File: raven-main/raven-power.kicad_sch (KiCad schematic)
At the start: 0 parts

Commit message: Added opamp circuits
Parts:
- added C10: 10uF, Capacitor_SMD:C_0402_1005Metric, symbol Device:C_Small
- added C11: 100nF, Capacitor_SMD:C_0402_1005Metric, symbol Device:C_Small
- added C12: 10nF, Capacitor_SMD:C_0402_1005Metric, symbol Device:C_Small
- added C4: 10pF, Capacitor_SMD:C_0402_1005Metric, symbol Device:C_Small
- added C5: 47uF, Capacitor_SMD:C_0402_1005Metric, symbol Device:C_Small
- added J1: XT60PW-M, AMASS_XT60PW-M, symbol iclr:XT60PW-M
- added R3: 226K, Resistor_SMD:R_0603_1608Metric, symbol Device:R
- added R4: 30k, Resistor_SMD:R_0603_1608Metric, symbol Device:R
- added R6: 31.6k, Resistor_SMD:R_0603_1608Metric, symbol Device:R
- added R7: 10k, Resistor_SMD:R_0603_1608Metric, symbol Device:R
- added U6: TPSM863257RDXR, RDX0007A-MFG, symbol TPSM863257RDXR:TPSM863257RDXR
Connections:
- new net: C12.1, R6.2, R7.1, U6.6 (EN)
- new net: C4.2, R3.2, R4.1, U6.7 (FB)
- new net 5V: C4.1, C5.1, R3.1, U6.3 (VOUT)
- new net BB_IN: C10.1, C11.1, J1.1 (+), R6.1, U6.1 (VIN)
- new net GND: C10.2, C11.2, C12.2, C5.2, J1.2 (-), R4.2, R7.2, U6.4 (PGND)
- no-connect marks 0 -> 2

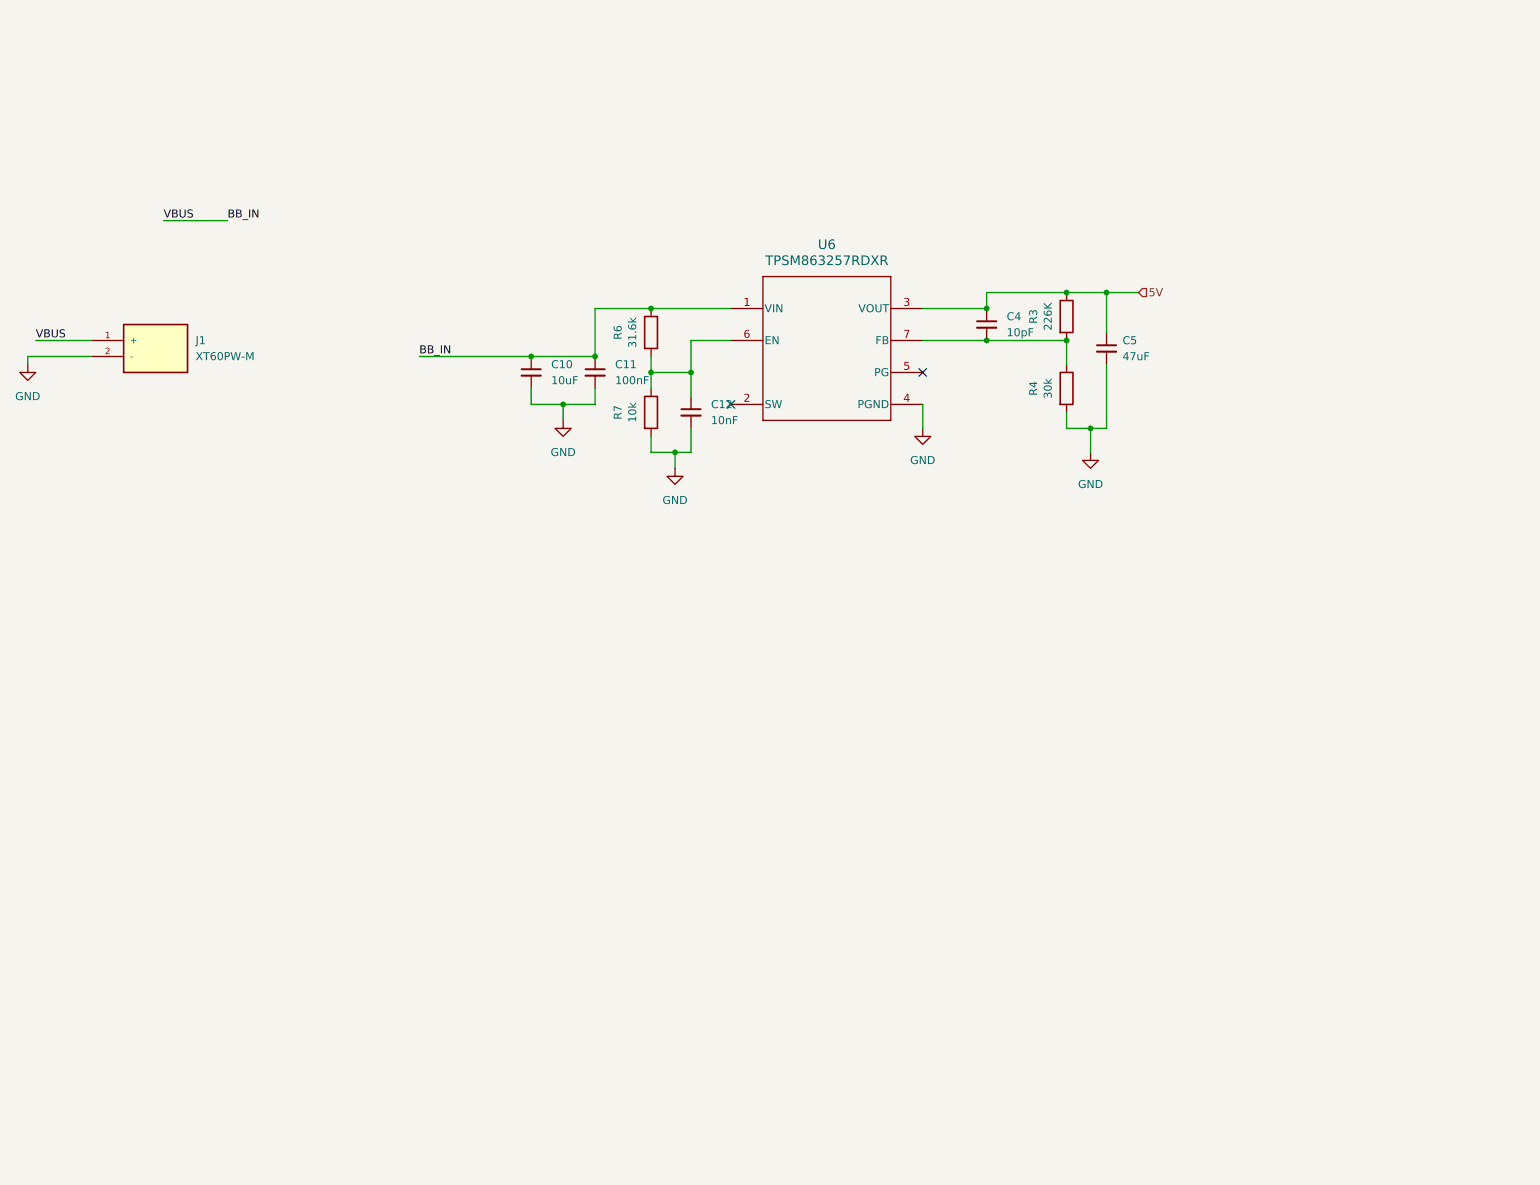
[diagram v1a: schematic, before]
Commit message: Added LDO Regulator
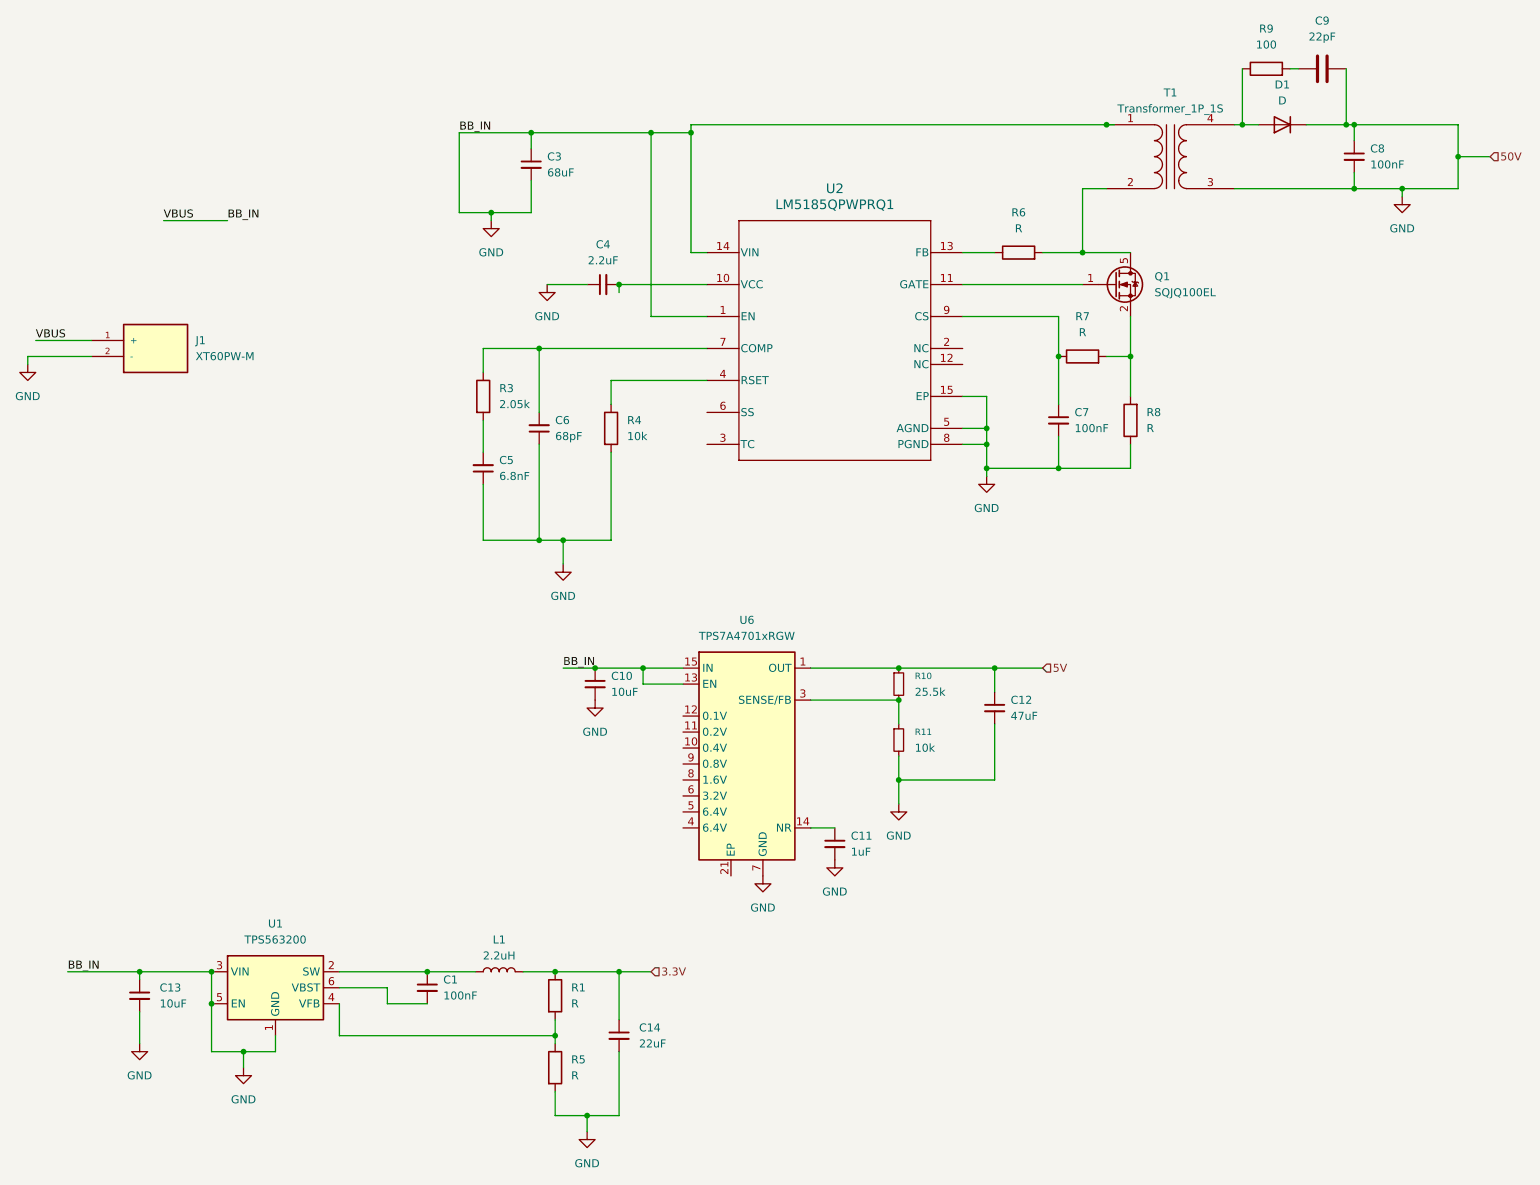
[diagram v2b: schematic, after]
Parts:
- removed U6: TPSM863257RDXR, RDX0007A-MFG, symbol TPSM863257RDXR:TPSM863257RDXR
- added C1, C7, C8: 100nF, symbol Device:C_Small
- added C13: 10uF, Capacitor_SMD:C_0402_1005Metric, symbol Device:C_Small
- added C14: 22uF, Capacitor_SMD:C_0402_1005Metric, symbol Device:C_Small
- added C3: 68uF, symbol Device:C_Small
- added C6: 68pF, symbol Device:C_Small
- added C9: 22pF, symbol Device:C
- added D1: D, symbol Device:D
- added L1: 2.2uH, symbol Device:L
- added Q1: SQJQ100EL, Package_TO_SOT_SMD:LFPAK88, symbol Transistor_FET:SQJQ100EL
- added R1, R5, R8: R, symbol Device:R
- added R10: 25.5k, symbol Device:R_Small
- added R11: 10k, symbol Device:R_Small
- added R9: 100, symbol Device:R
- added T1: Transformer_1P_1S, symbol Device:Transformer_1P_1S
- added U1: TPS563200, Package_TO_SOT_SMD:SOT-23-6, symbol Regulator_Switching:TPS563200
- added U2: LM5185QPWPRQ1, PWP0014G-IPC_A, symbol 2026-06-16_16-53-51:LM5185QPWPRQ1
- added U6: TPS7A4701xRGW, Package_DFN_QFN:Texas_RGW0020A_VQFN-20-1EP_5x5mm_P0.65mm_EP3.15x3.15mm_ThermalVias, symbol Regulator_Linear:TPS7A4701xRGW
- C10: footprint Capacitor_SMD:C_0402_1005Metric -> (none)
- C11: value 100nF -> 1uF; footprint Capacitor_SMD:C_0402_1005Metric -> (none)
- C12: value 10nF -> 47uF; footprint Capacitor_SMD:C_0402_1005Metric -> (none)
- C4: value 10pF -> 2.2uF; footprint Capacitor_SMD:C_0402_1005Metric -> (none)
- C5: value 47uF -> 6.8nF; footprint Capacitor_SMD:C_0402_1005Metric -> (none)
- R3: value 226K -> 2.05k; footprint Resistor_SMD:R_0603_1608Metric -> (none)
- R4: value 30k -> 10k; footprint Resistor_SMD:R_0603_1608Metric -> (none)
- R6: value 31.6k -> R; footprint Resistor_SMD:R_0603_1608Metric -> (none)
- R7: value 10k -> R; footprint Resistor_SMD:R_0603_1608Metric -> (none)
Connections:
- net 5V: now also C12.1, R10.1, U6.1 (OUT), U6.20 (OUT); no longer C4.1, C5.1, R3.1
- net GND: now also C10.1, C4.1, C5.1, J1.1 (+), C13.1, C13.2, C14.2, C3.1, C3.2, C6.1, C7.2, C8.1, C8.2, C9.2, D1.1 (K), R11.2, R5.2, R8.1, T1.1 (AA), T1.3 (SA), U1.1 (GND), U1.3 (VIN), U1.5 (EN), U2.1 (EN), U2.14 (VIN), U2.15 (EP), U2.5 (AGND), U2.8 (PGND), U6.13 (EN), U6.15 (IN), U6.16 (IN), U6.7 (GND); no longer C5.2, R7.2
- removed net BB_IN: C10.1, C11.1, J1.1 (+), R6.1
- new net: C6.2, R3.1, U2.7 (COMP)
- new net: D1.2 (A), R9.1, T1.4 (SB)
- new net: C9.1, R9.2
- new net: C7.1, R7.1, U2.9 (CS)
- new net: Q1.2 (S), Q1.3 (S), Q1.4 (S), R7.2, R8.2
- new net: R6.1, U2.13 (FB)
- new net: Q1.5 (D), R6.2, T1.2 (AB)
- new net: C5.2, R3.2
- new net: C4.2, U2.10 (VCC)
- new net: Q1.1 (G), U2.11 (GATE)
- new net: R4.1, U2.4 (RSET)
- new net: R10.2, R11.1, U6.3 (SENSE/FB)
- new net: R1.2, R5.1, U1.4 (VFB)
- new net: C1.1, L1.1, U1.2 (SW)
- new net: C1.2, U1.6 (VBST)
- new net: C11.1, U6.14 (NR)
- new net 3.3V: C14.1, L1.2, R1.1
- no-connect marks 2 -> 0
